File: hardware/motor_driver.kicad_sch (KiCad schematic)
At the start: 17 parts

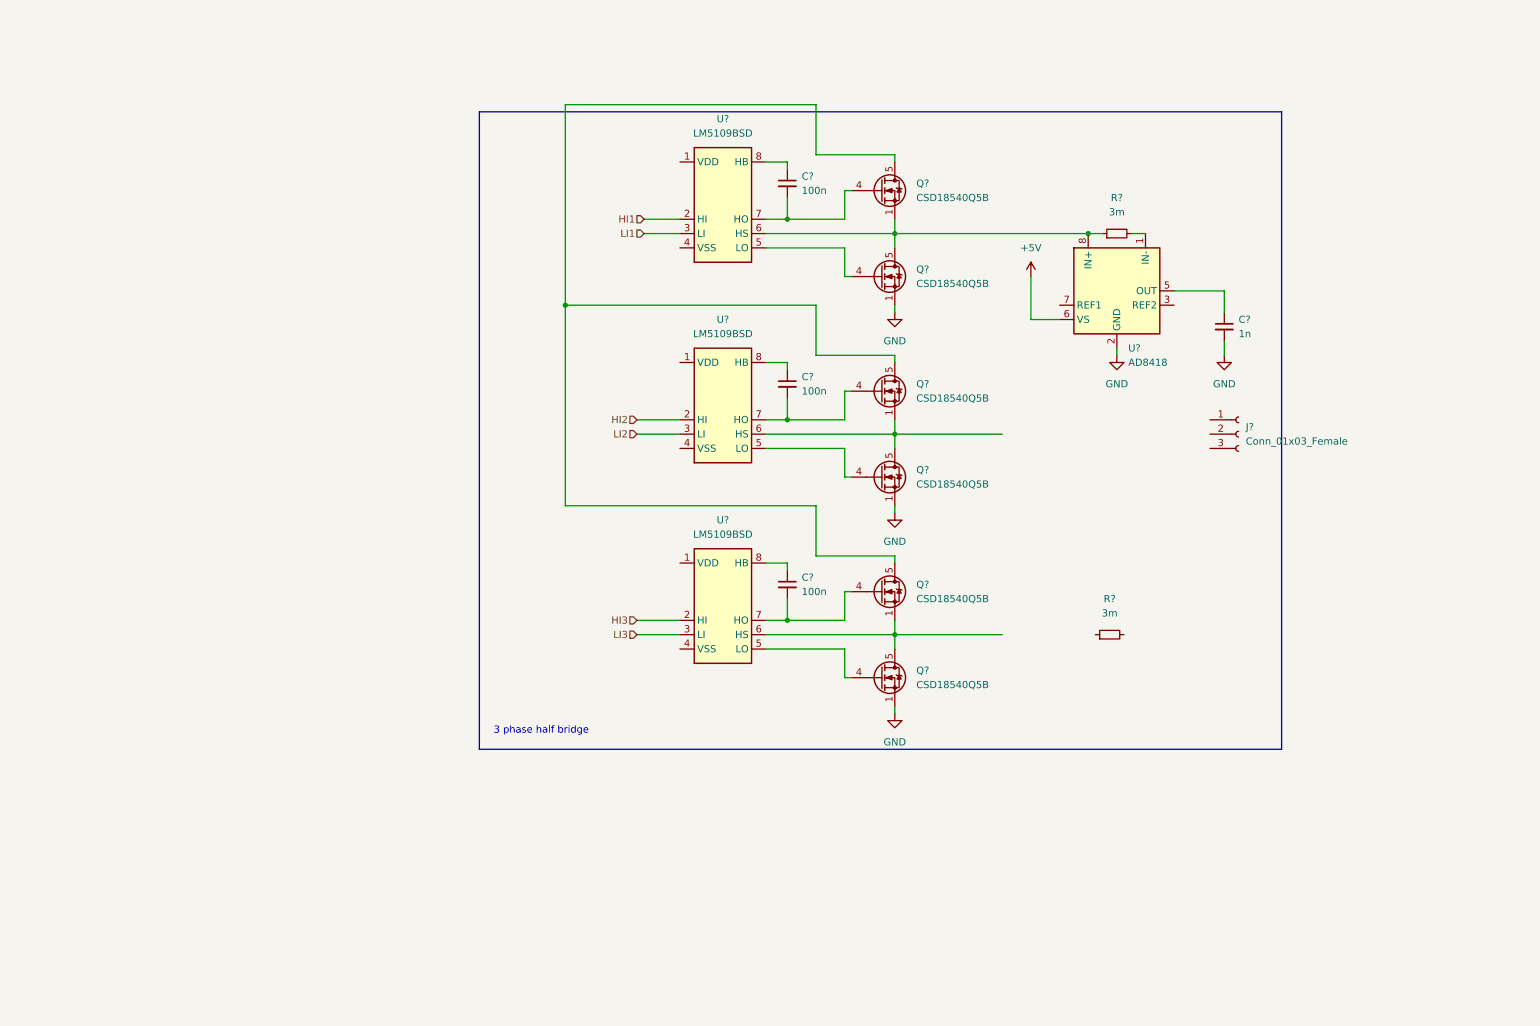
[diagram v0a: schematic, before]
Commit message: finish motor driver sch
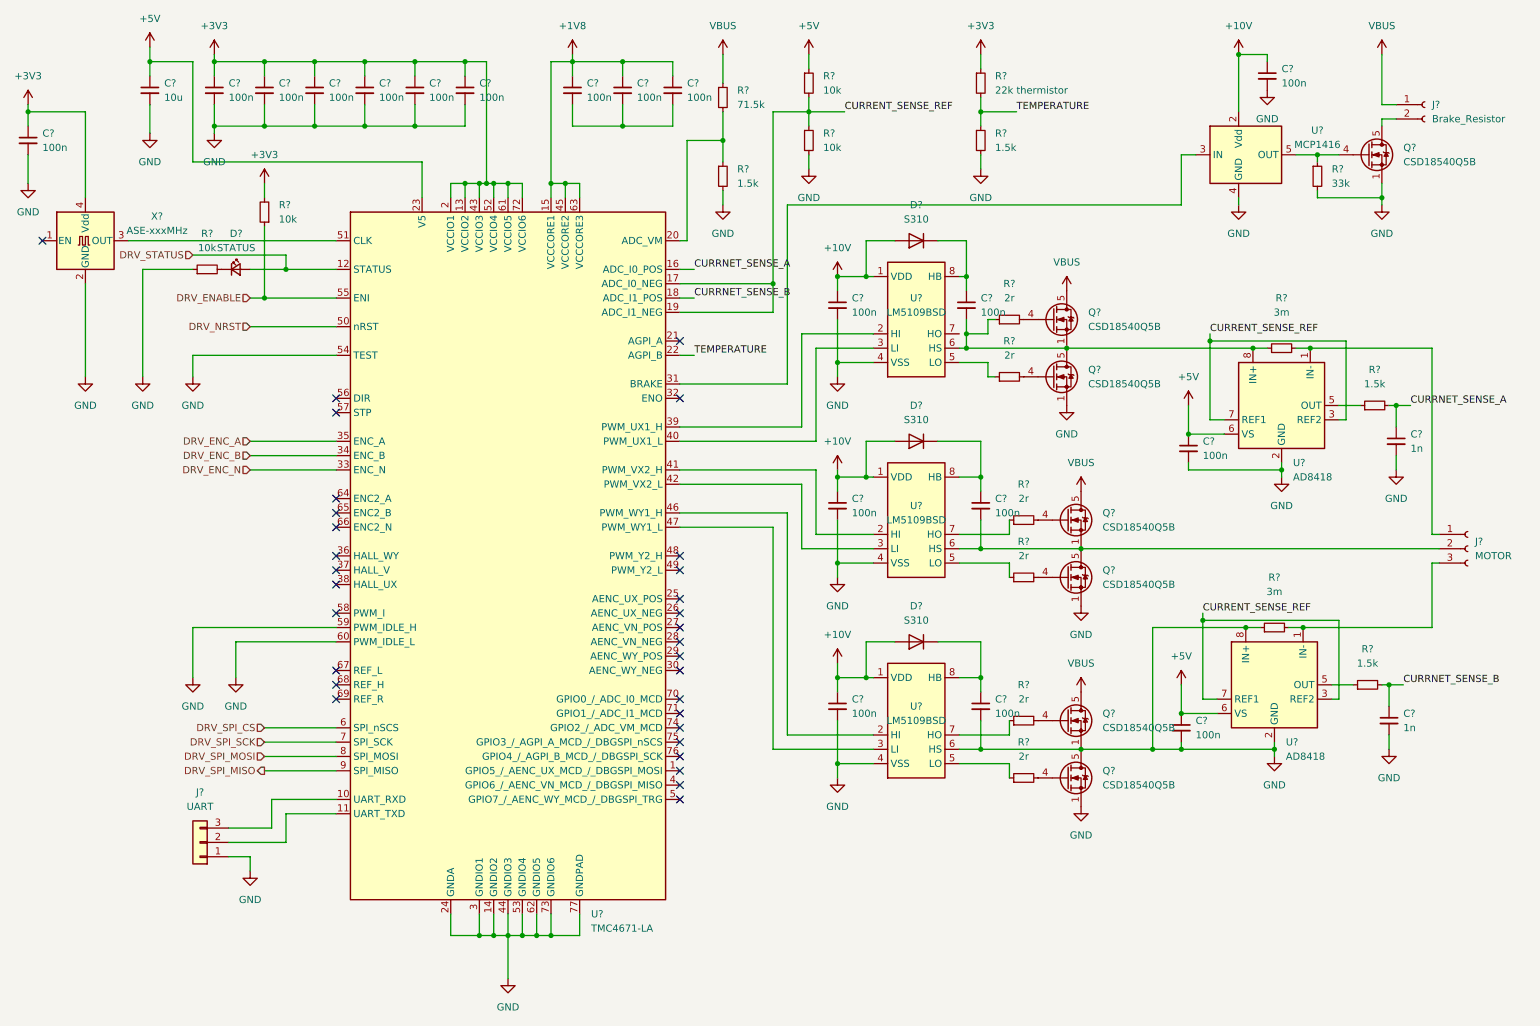
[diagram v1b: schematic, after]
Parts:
- removed Q? (x4): CSD18540Q5B, Package_TO_SOT_SMD:TDSON-8-1, symbol Transistor_FET:CSD18540Q5B
- removed R?: 3m, symbol Device:R_Small
- added C? (x16): 100n, symbol Device:C_Small
- added C?: 10u, symbol Device:C_Small
- added C?: 1n, symbol Device:C_Small
- added D?: STATUS, symbol Device:LED_Small
- added D? (x3): S310, Diode_THT:D_DO-41_SOD81_P10.16mm_Horizontal, symbol Diode:1N4007
- added J?: UART, symbol Connector_Generic:Conn_01x03
- added J?: Brake_Resistor, symbol Connector:Conn_01x02_Female
- added Q? (x5): CSD18540Q5B, Package_TO_SOT_SMD:TDSON-8-1, symbol Transistor_FET:CSD18540Q5B
- added R? (x4): 10k, symbol Device:R_Small
- added R?: 71.5k, symbol Device:R_Small
- added R? (x6): 2r, symbol Device:R_Small
- added R?: 3m, symbol Device:R_Small
- added R? (x4): 1.5k, symbol Device:R_Small
- added R?: 33k, symbol Device:R_Small
- added R?: 22k thermistor, symbol Device:R_Small
- added U?: MCP1416, Package_TO_SOT_SMD:SOT-23-5, symbol Driver_FET:MCP1416
- added U?: TMC4671-LA, Package_DFN_QFN:QFN-76-1EP_11.5x6.5mm_P0.4_EP9x5mm, symbol Driver_Motor:TMC4671-LA
- added U?: AD8418, symbol Amplifier_Current:AD8418
- added X?: ASE-xxxMHz, Oscillator:Oscillator_SMD_Abracon_ASE-4Pin_3.2x2.5mm, symbol Oscillator:ASE-xxxMHz
- J?: value Conn_01x03_Female -> MOTOR
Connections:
- net +5V: now also C?.1, C?.1, C?.1, R?.1, U?.23 (V5), U?.6 (VS)
- net GND: now also C?.2, U?.4 (VSS), U?.4 (VSS), U?.4 (VSS), U?.6 (HS), U?.9 (VSS), U?.9 (VSS), U?.9 (VSS), C?.2, C?.2, C?.2, C?.2, C?.2, C?.2, C?.2, C?.2, C?.2, C?.2, C?.2, C?.2, C?.2, C?.2, C?.2, J?.1 (Pin_1), Q?.1 (S), Q?.1 (S), Q?.1 (S), Q?.1 (S), Q?.2 (S), Q?.2 (S), Q?.2 (S), Q?.2 (S), Q?.3 (S), Q?.3 (S), Q?.3 (S), Q?.3 (S), Q?.5 (D), R?.1, R?.1, R?.2, R?.2, R?.2, R?.2, U?.14 (GNDIO2), U?.2 (GND), U?.24 (GNDA), U?.3 (GNDIO1), U?.4 (GND), U?.44 (GNDIO3), U?.53 (GNDIO4), U?.54 (TEST), U?.59 (PWM_IDLE_H), U?.60 (PWM_IDLE_L), U?.62 (GNDIO5), U?.73 (GNDIO6), U?.77 (GNDPAD), U?.8 (IN+), X?.2 (GND)
- net at C?.1, U?.8 (HB): now also D?.1 (K) (x3)
- net at U?.7 (HO): now also R?.1; no longer C?.2 (x2)
- net +10V: now reaches U?.1 (VDD)
- net +10V: now also U?.1 (VDD), U?.1 (VDD), C?.1, C?.1, C?.1, C?.1, D?.2 (A), D?.2 (A), D?.2 (A), U?.2 (Vdd)
- net at U?.5 (LO): now also R?.1 (x2)
- net at U?.6 (HS): now also C?.2, J?.2 (Pin_2), Q?.1 (S), Q?.2 (S), Q?.3 (S), Q?.5 (D)
- net at Q?.4 (G): now also R?.2; no longer U?.5 (LO)
- net at Q?.1 (S), Q?.2 (S), Q?.3 (S)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: now also C?.2, R?.1
- net at R?.2, U?.1 (IN-): now also J?.1 (Pin_1)
- net VBUS: now reaches Q?.5 (D)
- net VBUS: now also J?.1 (Pin_1), Q?.5 (D), Q?.5 (D), R?.1
- net at J?.3 (Pin_3): now also R?.2, U?.1 (IN-)
- net at U?.5 (OUT): now also R?.1; no longer C?.1
- net CURRENT_SENSE_REF: now reaches U?.3 (REF2)
- net CURRENT_SENSE_REF: now also U?.7 (REF1), R?.1, R?.2, U?.17 (ADC_I0_NEG), U?.19 (ADC_I1_NEG), U?.3 (REF2), U?.7 (REF1)
- net HI1: no longer names the net of U?.2 (HI)
- net HI1: now also U?.39 (PWM_UX1_H)
- net HI2: no longer names the net of U?.2 (HI)
- net HI2: now also U?.41 (PWM_VX2_H)
- net HI3: no longer names the net of U?.2 (HI)
- net HI3: now also U?.46 (PWM_WY1_H)
- net LI1: no longer names the net of U?.3 (LI)
- net LI1: now also U?.40 (PWM_UX1_L)
- net LI2: no longer names the net of U?.3 (LI)
- net LI2: now also U?.42 (PWM_VX2_L)
- net LI3: no longer names the net of U?.3 (LI)
- net LI3: now also U?.47 (PWM_WY1_L)
- new net: Q?.4 (G), R?.2 (x5)
- new net: D?.1 (K), R?.2
- new net: R?.1, R?.2, U?.20 (ADC_VM)
- new net: U?.3 (IN), U?.31 (BRAKE)
- new net: Q?.4 (G), R?.1, U?.5 (OUT)
- new net: J?.3 (Pin_3), U?.10 (UART_RXD)
- new net: J?.2 (Pin_2), U?.11 (UART_TXD)
- new net: U?.51 (CLK), X?.3 (OUT)
- new net: C?.2, C?.2, C?.2
- new net: R?.1, U?.5 (LO)
- new net: J?.2 (Pin_2), Q?.5 (D)
- new net: R?.1, U?.5 (OUT)
- new net +1V8: C?.1, C?.1, C?.1, U?.15 (VCCCORE1), U?.45 (VCCCORE2), U?.63 (VCCCORE3)
- new net +3V3: C?.1, C?.1, C?.1, C?.1, C?.1, C?.1, C?.1, R?.1, R?.2, U?.13 (VCCIO2), U?.2 (VCCIO1), U?.43 (VCCIO3), U?.52 (VCCIO4), U?.61 (VCCIO5), U?.72 (VCCIO6), X?.4 (Vdd)
- new net CURRNET_SENSE_A: C?.1, R?.2, U?.16 (ADC_I0_POS)
- new net CURRNET_SENSE_B: C?.1, R?.2, U?.18 (ADC_I1_POS)
- new net DRV_ENABLE: R?.1, U?.55 (ENI)
- new net DRV_ENC_A: U?.35 (ENC_A)
- new net DRV_ENC_B: U?.34 (ENC_B)
- new net DRV_ENC_N: U?.33 (ENC_N)
- new net DRV_NRST: U?.50 (nRST)
- new net DRV_SPI_CS: U?.6 (SPI_nSCS)
- new net DRV_SPI_MISO: U?.9 (SPI_MISO)
- new net DRV_SPI_MOSI: U?.8 (SPI_MOSI)
- new net DRV_SPI_SCK: U?.7 (SPI_SCK)
- new net DRV_STATUS: D?.2 (A), U?.12 (STATUS)
- new net TEMPERATURE: R?.1, R?.2, U?.22 (AGPI_B)
- now unconnected: U?.7 (HO)
- no-connect marks 0 -> 31
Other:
- note removed: "3 phase half bridge"
- moved on the sheet: C?, J?, Q?, R?, U?

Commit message: add firmware
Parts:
- C30, C31, C32, C33, C34, C35, C36, C37, C38, C39, C40, C41, C42, C43, C44, C45, C46, C47, C48, C49, C50, C51: renamed from C?; footprint (none) -> Capacitor_SMD:C_0402_1005Metric
- D3, D5: renamed from D?; footprint Diode_THT:D_DO-41_SOD81_P10.16mm_Horizontal -> (none)
- gave numbers to parts that had none: 39
